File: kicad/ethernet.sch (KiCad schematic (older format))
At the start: 6 parts, among them J1 RJ45_Abracon_ARJP11A-MASA-B-A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, J2 Conn_01x04_Male, J3 Conn_01x04_Male, J4 Conn_01x04_Male, J5 Conn_01x04_Male, U1 MSP432E401Y

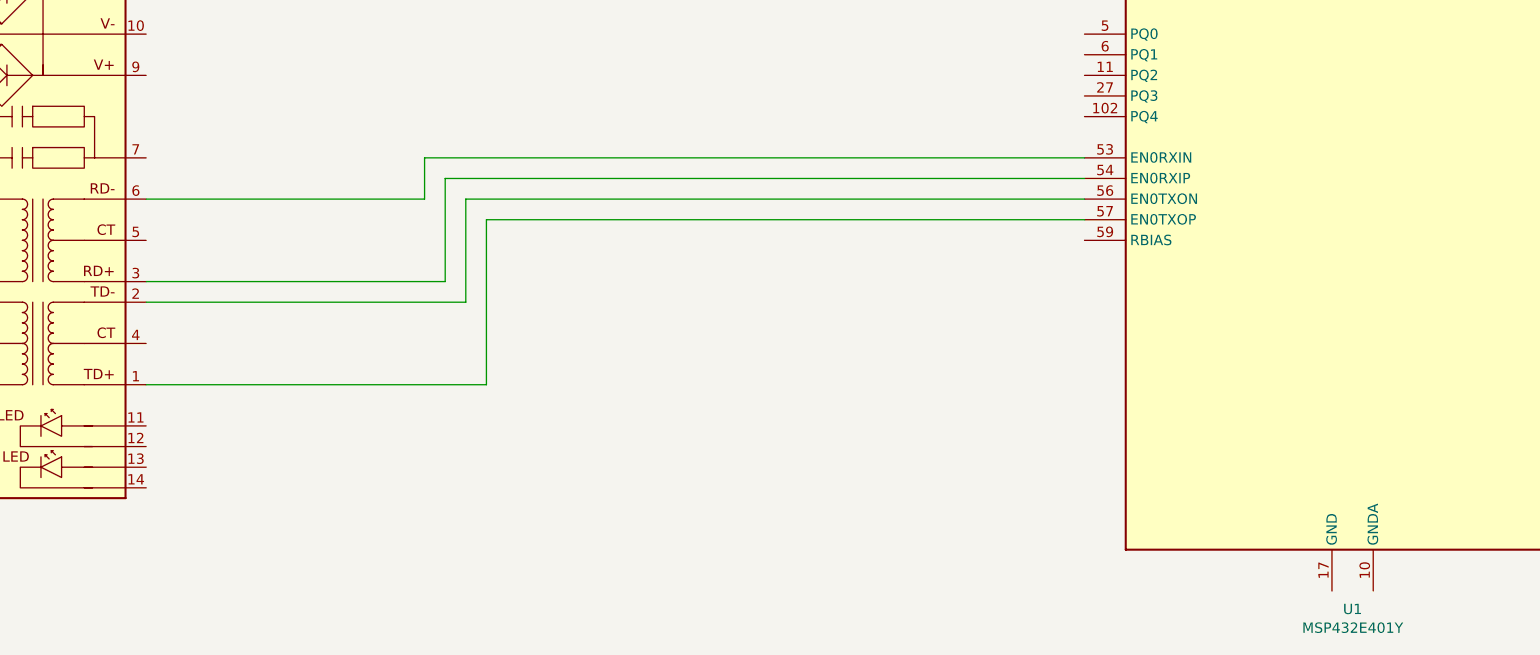
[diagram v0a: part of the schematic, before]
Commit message: working on ethernet board
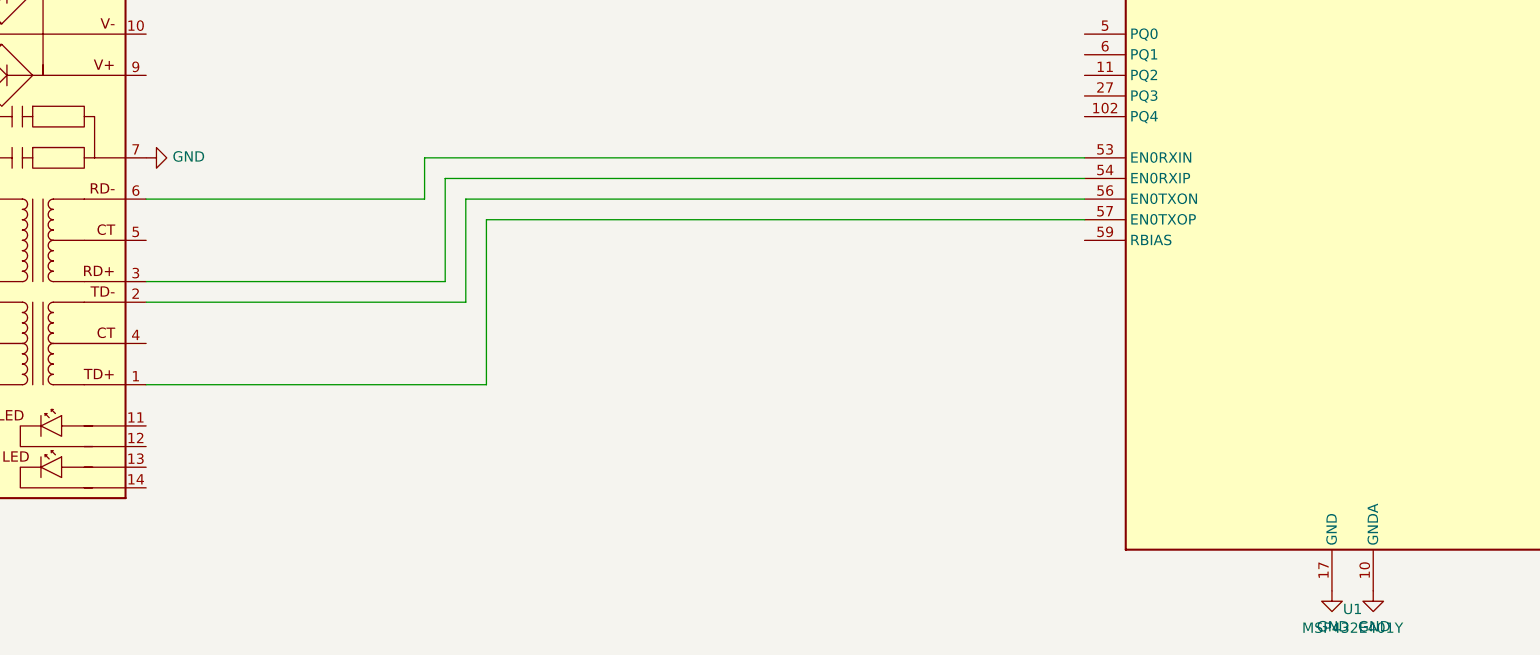
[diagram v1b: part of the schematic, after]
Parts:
- J2, J3, J4, J5: footprint (none) -> Connector_PinHeader_2.54mm:PinHeader_1x04_P2.54mm_Vertical
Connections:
- net GND: now reaches J1.7
- net GND: now also U1.10 (GNDA), U1.114 (GND), U1.17 (GND), U1.48 (GND), U1.55 (GND), U1.58 (GND), U1.80 (GND)
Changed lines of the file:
@@
 F 0 "J2" H 13508 1881 50  0000 C CNN
 F 1 "Conn_01x04_Male" H 13508 1790 50  0000 C CNN
-F 2 "" H 13400 1600 50  0001 C CNN
+F 2 "Connector_PinHeader_2.54mm:PinHeader_1x04_P2.54mm_Vertical" H 13400 1600 50  0001 C CNN
 F 3 "~" H 13400 1600 50  0001 C CNN
 	1    13400 1600
@@
 F 0 "J4" H 14408 1881 50  0000 C CNN
 F 1 "Conn_01x04_Male" H 14408 1790 50  0000 C CNN
-F 2 "" H 14300 1600 50  0001 C CNN
+F 2 "Connector_PinHeader_2.54mm:PinHeader_1x04_P2.54mm_Vertical" H 14300 1600 50  0001 C CNN
 F 3 "~" H 14300 1600 50  0001 C CNN
 	1    14300 1600
@@
 F 0 "J5" H 14408 2631 50  0000 C CNN
 F 1 "Conn_01x04_Male" H 14408 2540 50  0000 C CNN
-F 2 "" H 14300 2350 50  0001 C CNN
+F 2 "Connector_PinHeader_2.54mm:PinHeader_1x04_P2.54mm_Vertical" H 14300 2350 50  0001 C CNN
 F 3 "~" H 14300 2350 50  0001 C CNN
 	1    14300 2350
@@
 F 0 "J3" H 13508 2631 50  0000 C CNN
 F 1 "Conn_01x04_Male" H 13508 2540 50  0000 C CNN
-F 2 "" H 13400 2350 50  0001 C CNN
+F 2 "Connector_PinHeader_2.54mm:PinHeader_1x04_P2.54mm_Vertical" H 13400 2350 50  0001 C CNN
 F 3 "~" H 13400 2350 50  0001 C CNN
 	1    13400 2350
@@
 Wire Wire Line
 	3850 6700 6750 6700
+$Comp
+L power:GND #PWR?
+U 1 1 6113EFB9
+P 2200 6400
+F 0 "#PWR?" H 2200 6150 50  0001 C CNN
+F 1 "GND" V 2205 6272 50  0000 R CNN
+F 2 "" H 2200 6400 50  0001 C CNN
+F 3 "" H 2200 6400 50  0001 C CNN
+	1    2200 6400
+	0    -1   -1   0
+$EndComp
+$Comp
+L power:GND #PWR?
+U 1 1 61143832
+P 7950 8500
+F 0 "#PWR?" H 7950 8250 50  0001 C CNN
+F 1 "GND" H 7955 8327 50  0000 C CNN
+F 2 "" H 7950 8500 50  0001 C CNN
+F 3 "" H 7950 8500 50  0001 C CNN
+	1    7950 8500
+	1    0    0    -1
+$EndComp
+$Comp
+L power:GND #PWR?
+U 1 1 6114407E
+P 8150 8500
+F 0 "#PWR?" H 8150 8250 50  0001 C CNN
+F 1 "GND" H 8155 8327 50  0000 C CNN
+F 2 "" H 8150 8500 50  0001 C CNN
+F 3 "" H 8150 8500 50  0001 C CNN
+	1    8150 8500
+	1    0    0    -1
+$EndComp
 $EndSCHEMATC

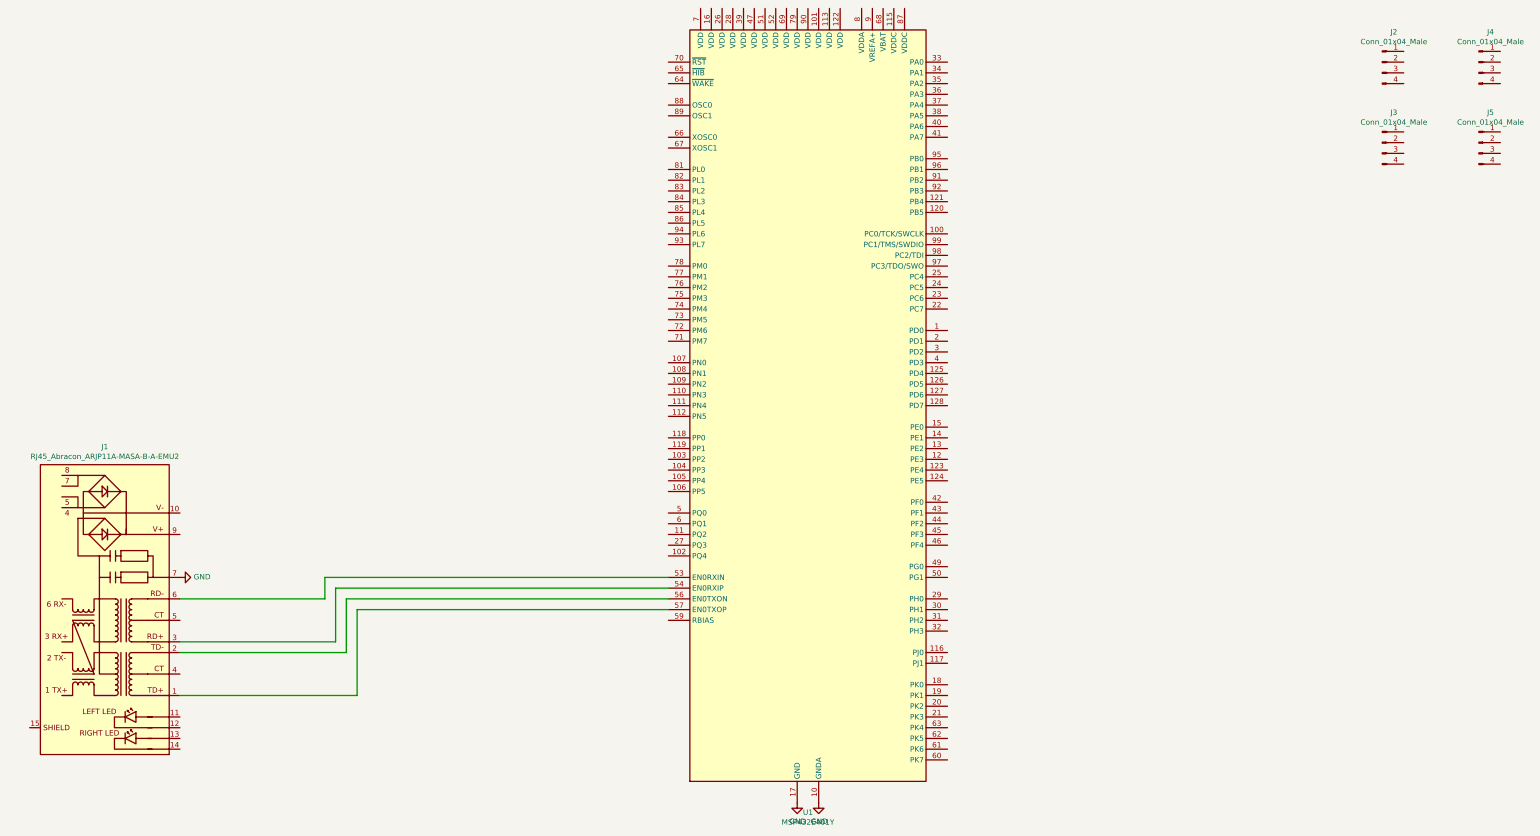
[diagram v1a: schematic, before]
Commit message: add QSPI flash to ethernet board
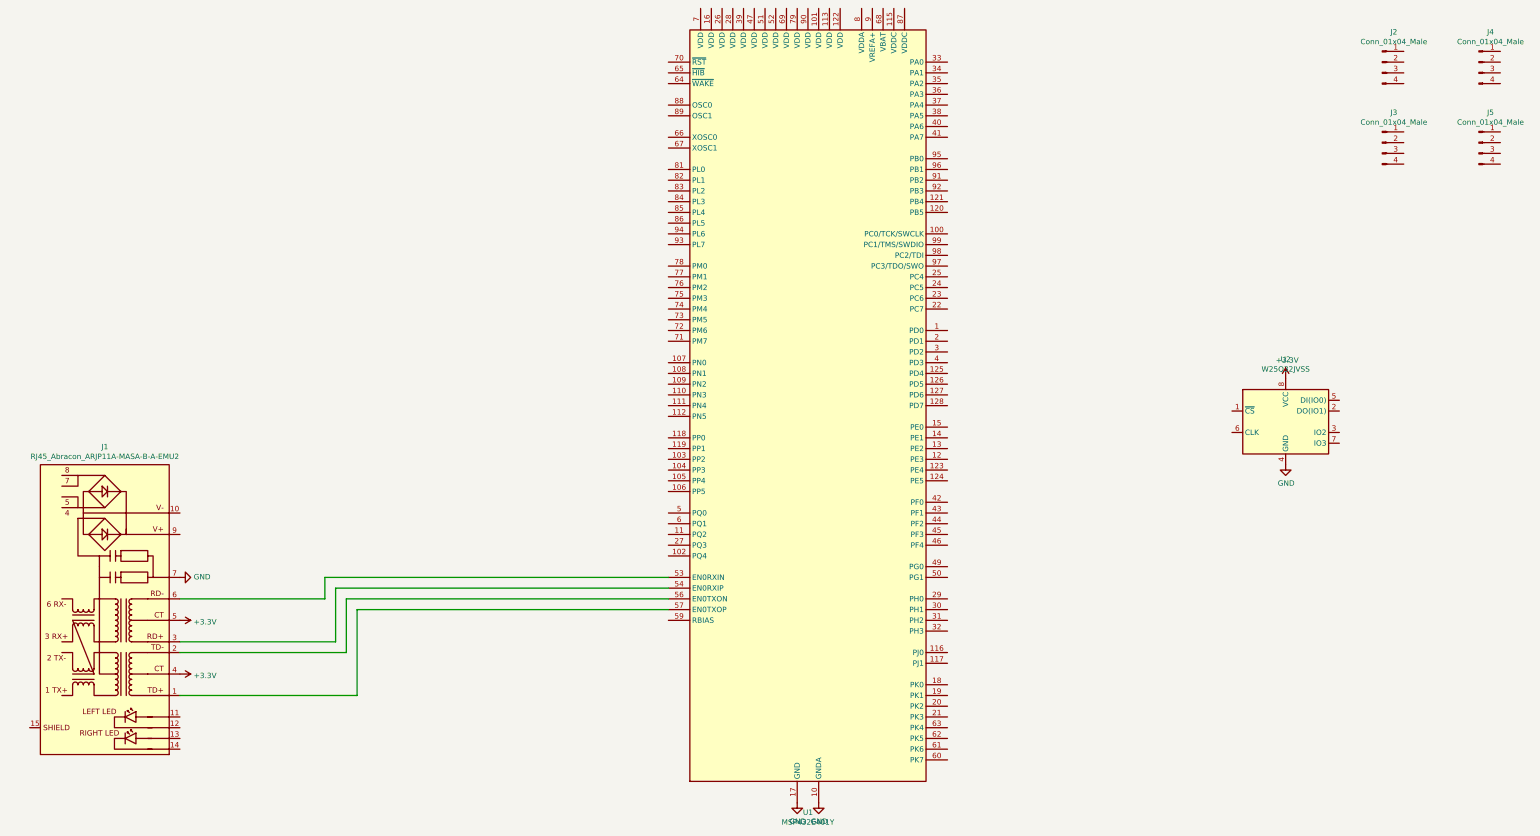
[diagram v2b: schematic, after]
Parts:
- added U2: W25Q32JVSS, Package_SO:SOIC-8_5.23x5.23mm_P1.27mm, symbol Memory_Flash:W25Q32JVSS
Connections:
- net GND: now also U2.4 (GND)
- net +3V3: now reaches J1.4 (CT)
- net +3V3: now also J1.5 (CT), U2.8 (VCC)
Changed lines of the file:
@@
 	3850 6700 6750 6700
 $Comp
-L power:GND #PWR?
+L power:GND #PWR0101
 U 1 1 6113EFB9
 P 2200 6400
-F 0 "#PWR?" H 2200 6150 50  0001 C CNN
+F 0 "#PWR0101" H 2200 6150 50  0001 C CNN
 F 1 "GND" V 2205 6272 50  0000 R CNN
 F 2 "" H 2200 6400 50  0001 C CNN
@@
 $EndComp
 $Comp
-L power:GND #PWR?
+L power:GND #PWR0102
 U 1 1 61143832
 P 7950 8500
-F 0 "#PWR?" H 7950 8250 50  0001 C CNN
+F 0 "#PWR0102" H 7950 8250 50  0001 C CNN
 F 1 "GND" H 7955 8327 50  0000 C CNN
 F 2 "" H 7950 8500 50  0001 C CNN
@@
 $EndComp
 $Comp
-L power:GND #PWR?
+L power:GND #PWR0103
 U 1 1 6114407E
 P 8150 8500
-F 0 "#PWR?" H 8150 8250 50  0001 C CNN
+F 0 "#PWR0103" H 8150 8250 50  0001 C CNN
 F 1 "GND" H 8155 8327 50  0000 C CNN
 F 2 "" H 8150 8500 50  0001 C CNN
@@
 	1    0    0    -1
 $EndComp
+$Comp
+L Memory_Flash:W25Q32JVSS U2
+U 1 1 61142364
+P 12500 4950
+F 0 "U2" H 12500 5531 50  0000 C CNN
+F 1 "W25Q32JVSS" H 12500 5440 50  0000 C CNN
+F 2 "Package_SO:SOIC-8_5.23x5.23mm_P1.27mm" H 12500 4950 50  0001 C CNN
+F 3 "http://www.winbond.com/resource-files/w25q32jv%20revg%2003272018%20plus.pdf" H 12500 4950 50  0001 C CNN
+	1    12500 4950
+	1    0    0    -1
+$EndComp
+$Comp
+L power:GND #PWR0104
+U 1 1 61142971
+P 12500 5350
+F 0 "#PWR0104" H 12500 5100 50  0001 C CNN
+F 1 "GND" H 12505 5177 50  0000 C CNN
+F 2 "" H 12500 5350 50  0001 C CNN
+F 3 "" H 12500 5350 50  0001 C CNN
+	1    12500 5350
+	1    0    0    -1
+$EndComp
+$Comp
+L power:+3.3V #PWR0105
+U 1 1 61143640
+P 12500 4550
+F 0 "#PWR0105" H 12500 4400 50  0001 C CNN
+F 1 "+3.3V" H 12515 4723 50  0000 C CNN
+F 2 "" H 12500 4550 50  0001 C CNN
+F 3 "" H 12500 4550 50  0001 C CNN
+	1    12500 4550
+	1    0    0    -1
+$EndComp
+$Comp
+L power:+3.3V #PWR0106
+U 1 1 61143B02
+P 2200 6800
+F 0 "#PWR0106" H 2200 6650 50  0001 C CNN
+F 1 "+3.3V" V 2215 6928 50  0000 L CNN
+F 2 "" H 2200 6800 50  0001 C CNN
+F 3 "" H 2200 6800 50  0001 C CNN
+	1    2200 6800
+	0    1    1    0
+$EndComp
+$Comp
+L power:+3.3V #PWR0107
+U 1 1 611442EF
+P 2200 7300
+F 0 "#PWR0107" H 2200 7150 50  0001 C CNN
+F 1 "+3.3V" V 2215 7428 50  0000 L CNN
+F 2 "" H 2200 7300 50  0001 C CNN
+F 3 "" H 2200 7300 50  0001 C CNN
+	1    2200 7300
+	0    1    1    0
+$EndComp
 $EndSCHEMATC
